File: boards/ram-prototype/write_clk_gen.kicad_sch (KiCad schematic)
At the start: 24 parts, among them U1 74LVC1G00, U2 74LVC1G00, U3 74LVC1G00, U4 74LVC1G00, U5 74LVC1G00, U6 74LVC1G00, U7 74LVC1G00, U8 74LVC1G00

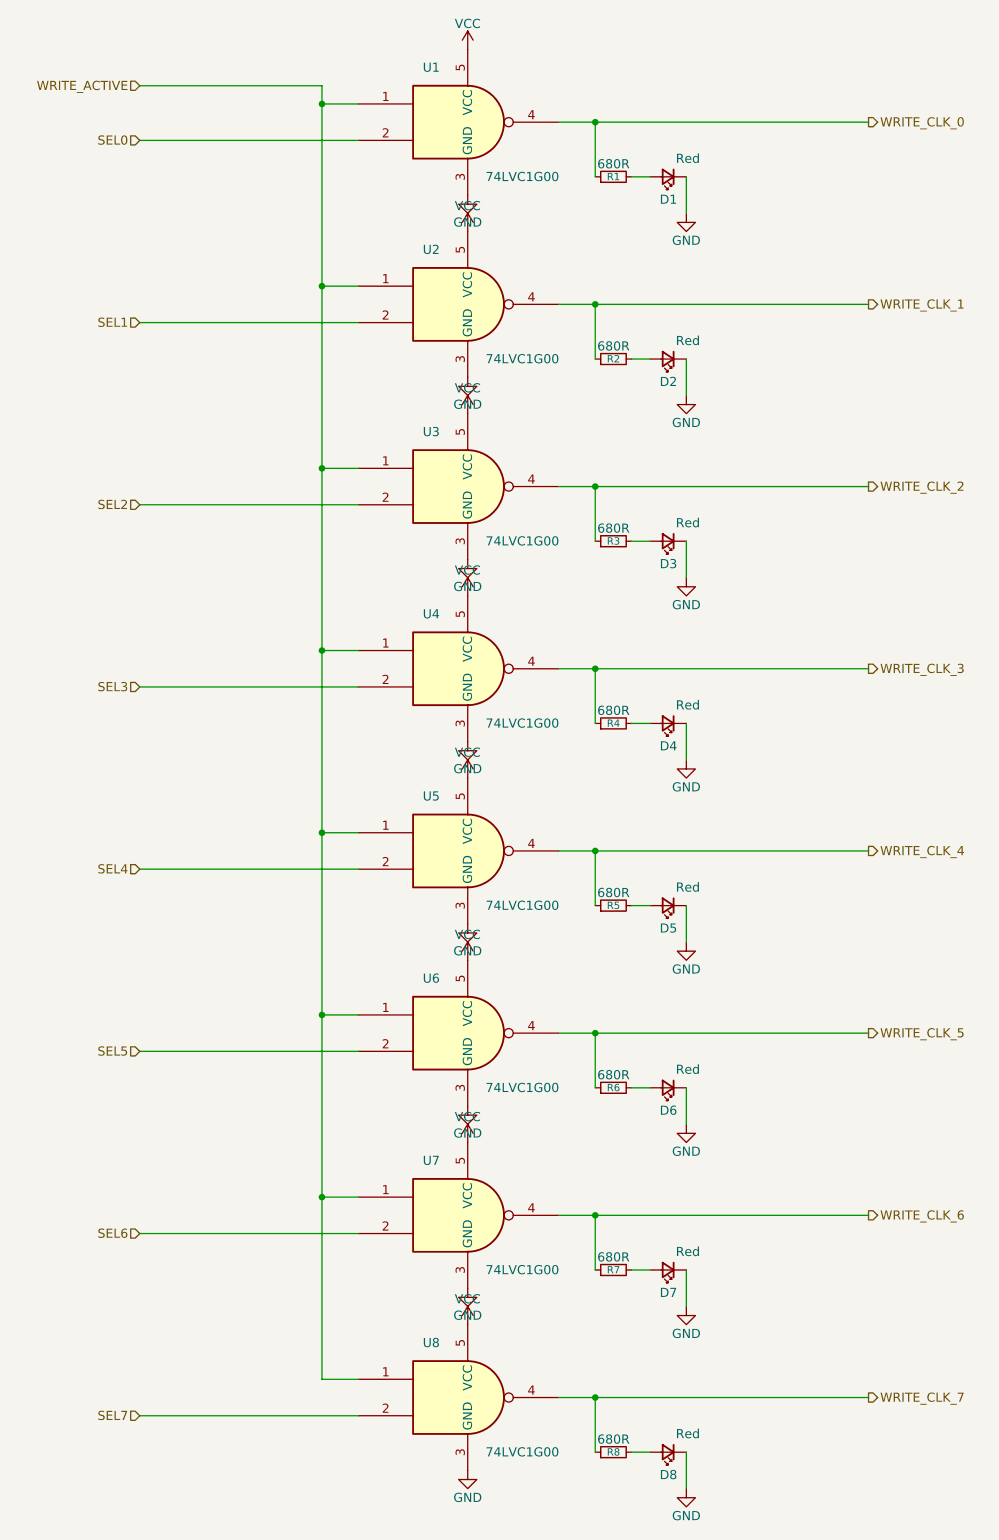
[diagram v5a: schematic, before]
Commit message: fix many issues
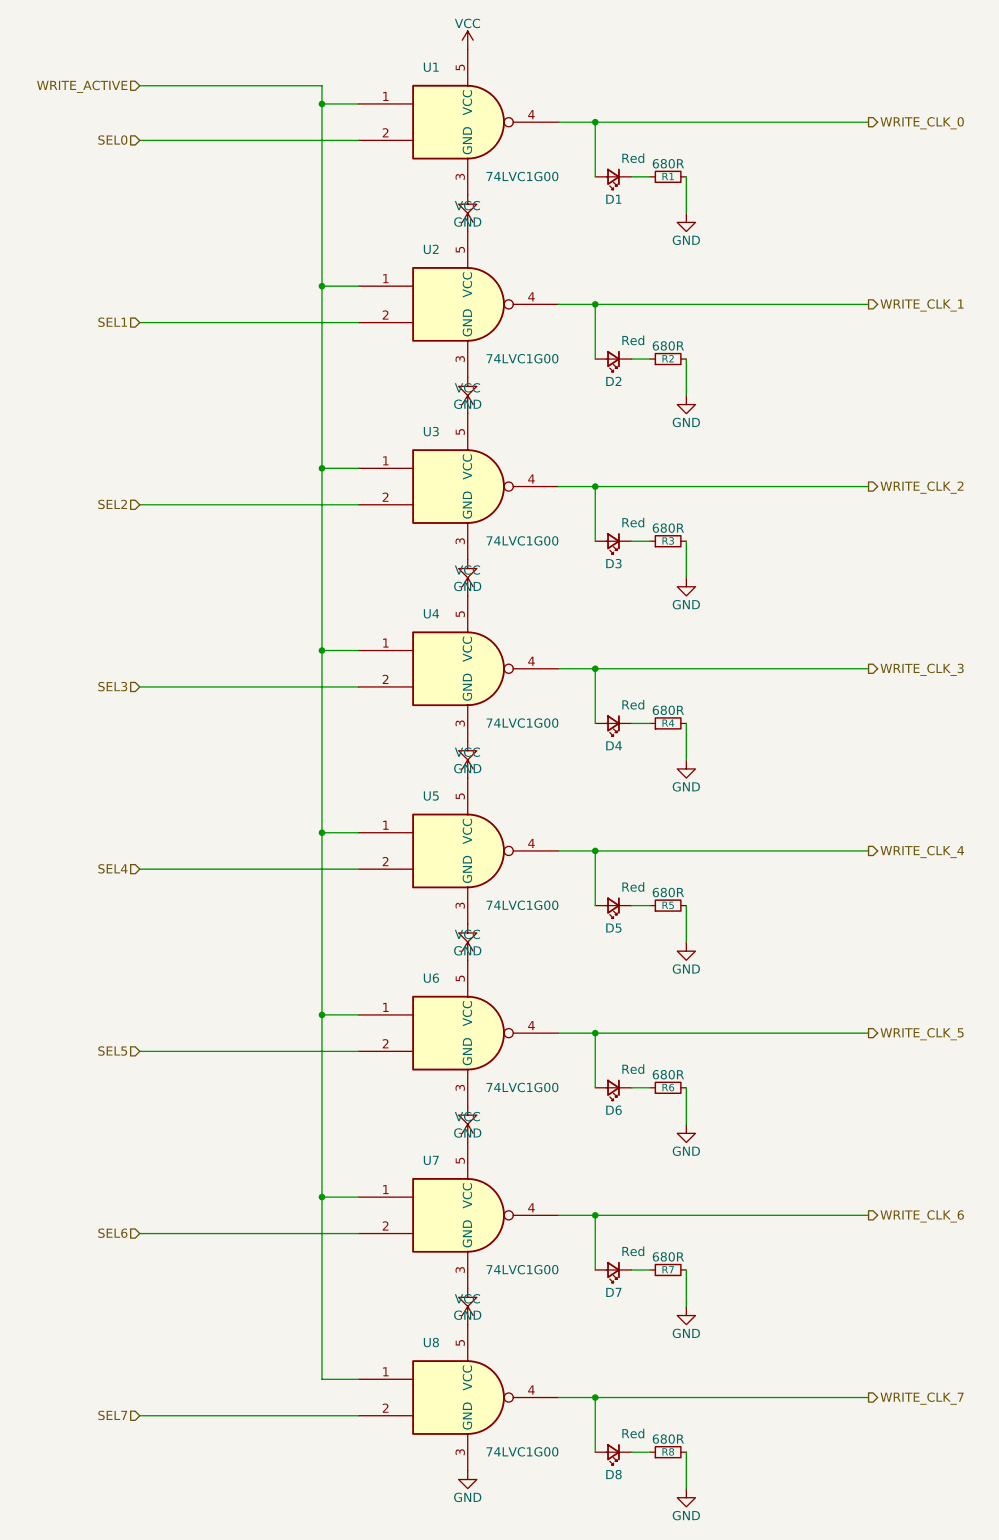
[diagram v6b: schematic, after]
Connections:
- net GND: now also R1.2, R2.2, R3.2, R4.2, R5.2, R6.2, R7.2, R8.2; no longer D1.1 (K), D2.1 (K), D3.1 (K), D4.1 (K), D5.1 (K), D6.1 (K), D7.1 (K), D8.1 (K)
- net WRITE_CLK_0: now also D1.2 (A); no longer R1.1
- net WRITE_CLK_1: now also D2.2 (A); no longer R2.1
- net WRITE_CLK_2: now also D3.2 (A); no longer R3.1
- net WRITE_CLK_3: now also D4.2 (A); no longer R4.1
- net WRITE_CLK_4: now also D5.2 (A); no longer R5.1
- net WRITE_CLK_5: now also D6.2 (A); no longer R6.1
- net WRITE_CLK_6: now also D7.2 (A); no longer R7.1
- net WRITE_CLK_7: now also D8.2 (A); no longer R8.1
- new net: D1.1 (K), R1.1
- new net: D3.1 (K), R3.1
- new net: D5.1 (K), R5.1
- new net: D6.1 (K), R6.1
- new net: D7.1 (K), R7.1
- new net: D4.1 (K), R4.1
- new net: D8.1 (K), R8.1
- new net: D2.1 (K), R2.1
